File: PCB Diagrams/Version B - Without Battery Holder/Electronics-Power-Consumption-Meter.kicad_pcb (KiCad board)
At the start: 2 copper layers, 88.9 x 96.5 mm, 35 parts, among them J1 Jack_DC, J10 01x02, J11 01x02, J12 01x02, J13 01x02, J2 01x02, J3 01x02, J4 USB_A, J5 Jack_DC, J6 Jack_DC, J7 USB_B_Mini, J8 USB_B_Micro, J9 01x04, SW1 SW_SPDT, SW2 SW_Push, U1 INA219_Module, U2 Display_5641BS

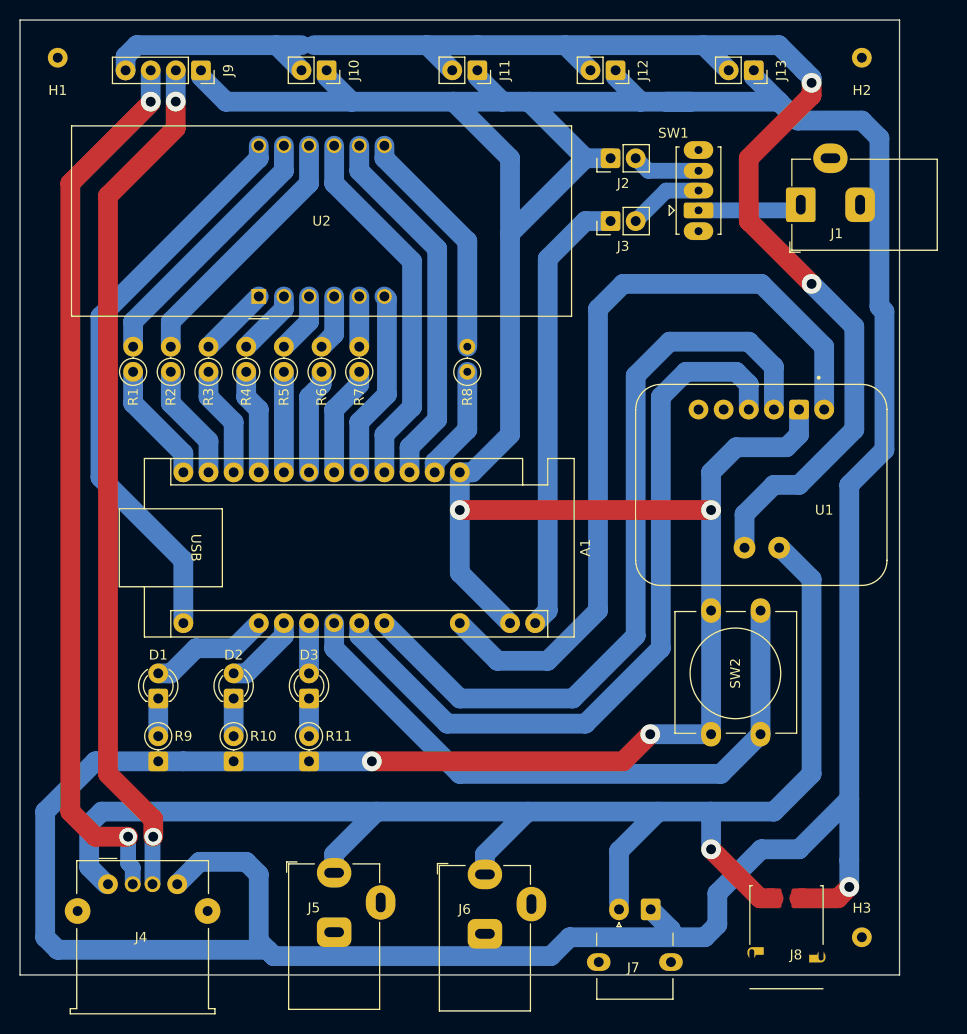
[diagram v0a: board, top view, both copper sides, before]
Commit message: Adding case 3D model
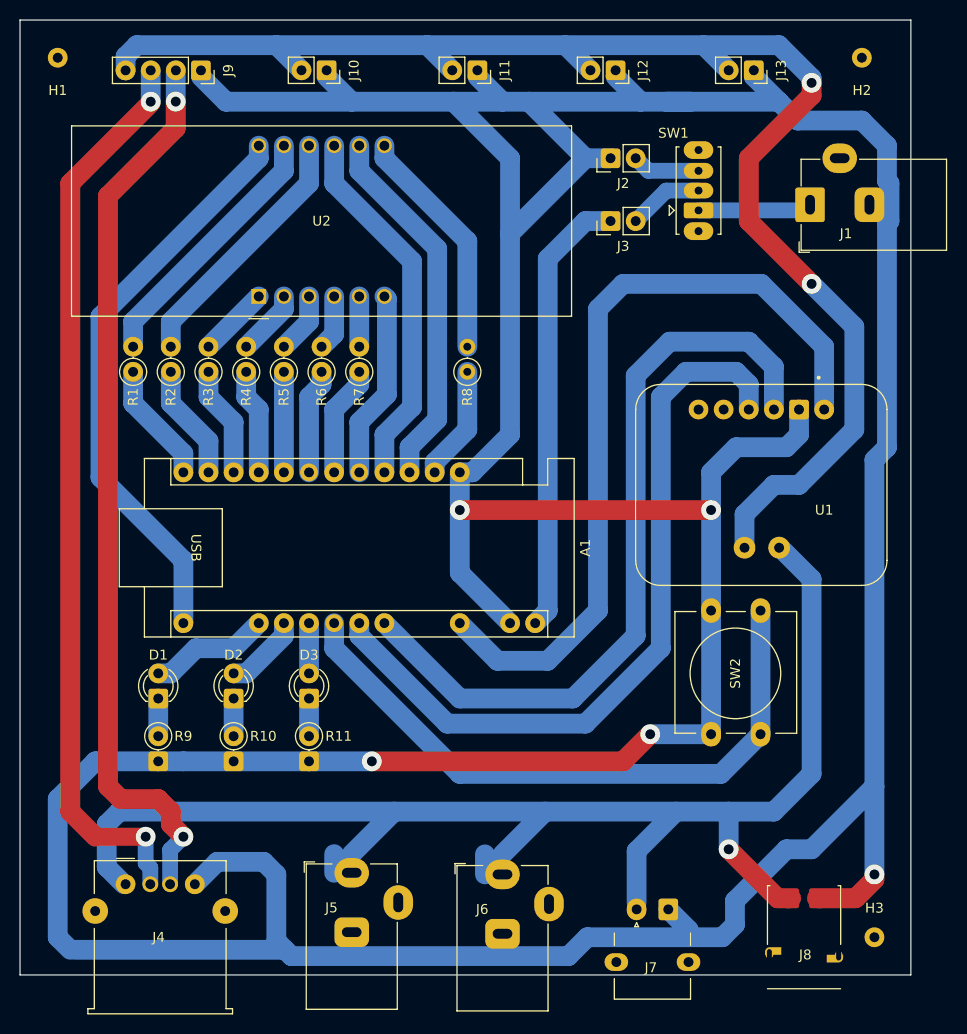
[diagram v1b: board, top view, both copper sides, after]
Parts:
- moved J6 1.78 mm to (145.3, 119.4)
- moved J4 1.78 mm to (107.2, 120.4)
- moved J5 1.78 mm to (130.0, 119.2)
- moved J7 1.78 mm to (158.8, 123.2)
- moved J8 1.78 mm to (175.8, 127.5)
- moved H3 1.27 mm to (182.9, 125.7)
- moved J1 0.94 mm to (176.4, 51.7)
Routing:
- net DATA1+: track 87.0 -> 91.1 mm
- net VIN+: track 145.4 -> 143.6 mm
- net DATA1-: track 90.2 -> 92.0 mm
- net VIN-: track 146.3 -> 147.6 mm
- net Net-(SW1-A): track 10.6 -> 11.5 mm
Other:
- board size 88.9 x 96.5 mm -> 90 x 96.5 mm
